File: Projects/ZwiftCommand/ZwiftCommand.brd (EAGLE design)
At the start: 47.4 x 21.2 mm, 17 parts, among them M1 DMP2165UW, U1 BAT-HLD-001-THM

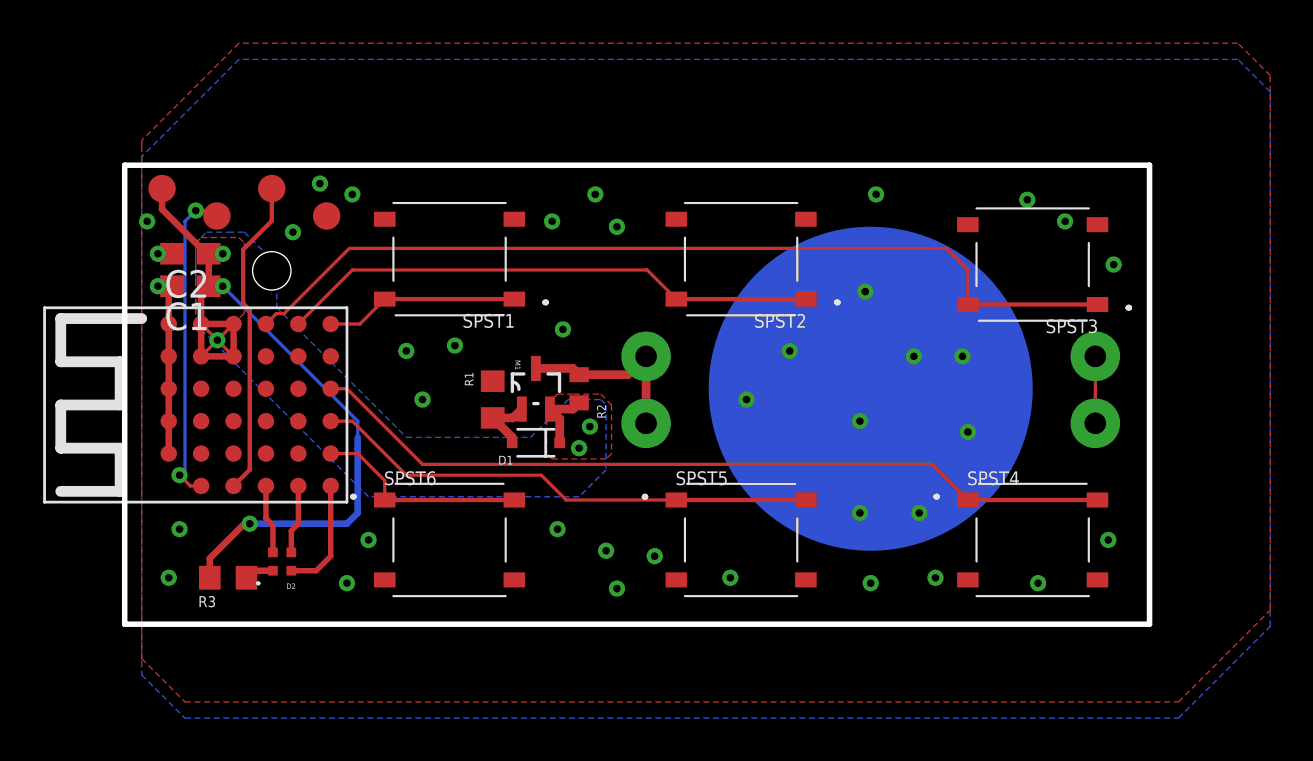
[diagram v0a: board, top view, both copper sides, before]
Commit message: ZwiftCommand with nRF52
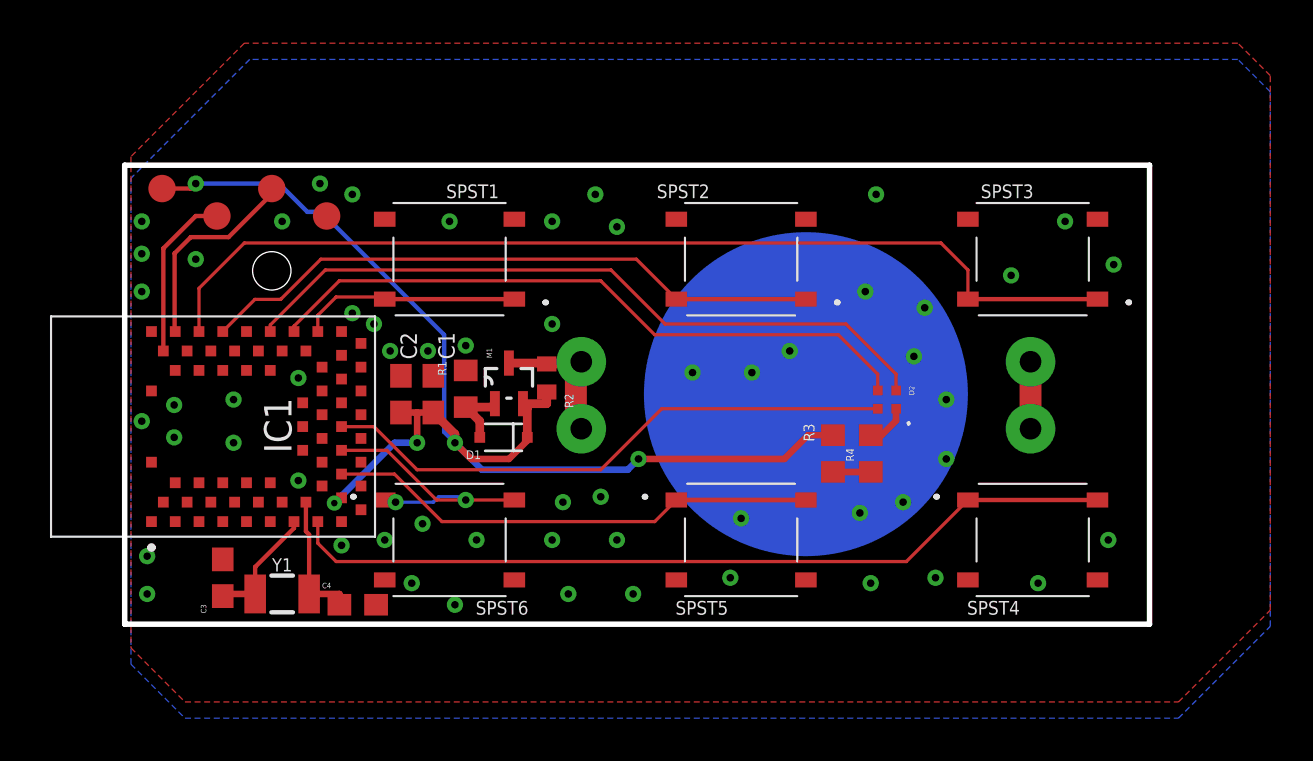
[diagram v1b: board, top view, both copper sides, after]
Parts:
- removed U$1: N5150, N5:N5150
- added C3, C4: (no value), resistor:C0603
- added IC1: BMD-340-A-R, Rigado:BMD340AR
- added R4: 300, resistor:R0603
- added Y1: 32.768kHz, SparkFun-Clocks:CRYSTAL-SMD-3.2X1.5MM
- moved D2 29.0 mm to (27.2, 12.5), turned to 270 degrees
- moved R3 28.6 mm to (24.8, 10.0), turned to 270 degrees
- moved C1 12.3 mm to (6.25, 12.8), turned to 90 degrees
- moved C2 11.7 mm to (4.75, 12.8), turned to 90 degrees
- moved U1 3.01 mm to (23.5, 12.8)
- moved R2 1.58 mm to (11.5, 13.5)
- moved D1 1.52 mm to (9.50, 10.8)
- moved R1 1.35 mm to (7.75, 13.0)
- moved M1 1.27 mm to (9.75, 13.2)
- moved SPST3 0.25 mm to (34.0, 19.0)
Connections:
- new net N$1: C3.1, IC1.13, Y1.P$1
- new net N$4: C4.1, IC1.14, Y1.P$2
- new net N$5: D2.1, R4.2
- net BTN1: now also IC1.31; no longer U$1.F6
- net BTN2: now also IC1.39; no longer U$1.E6
- net BTN3: now also IC1.41; no longer U$1.D6
- net BTN4: now also IC1.15; no longer U$1.F4
- net BTN5: now also IC1.19; no longer U$1.F3
- net BTN6: now also IC1.21; no longer U$1.F2
- net GND: now also C3.2, C4.2, IC1.1, IC1.16, IC1.18, IC1.2, IC1.29, IC1.3, IC1.30, IC1.4, IC1.45, IC1.46, IC1.47, IC1.5, IC1.55; no longer U$1.A2, U$1.A3, U$1.A4, U$1.A5, U$1.A6
- net LEDB: now also IC1.35; no longer U$1.F1
- net LEDG: now also IC1.33; no longer U$1.E1
- net LEDR: now also IC1.23; no longer U$1.D1
- net N$3: now also R4.1; no longer D2.1
- net SWDCLK: now also IC1.43; no longer U$1.C1
- net SWDIO: now also IC1.44; no longer U$1.B1
- net VDD: now also IC1.17; no longer U$1.B5, U$1.B6, U$1.C5, U$1.C6
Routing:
- net LEDB: track 5.35 -> 33.1 mm
- net LEDG: track 3.21 -> 30.7 mm
- net LEDR: track 3.21 -> 26.8 mm
- net VDD: track 43.0 -> 57.7 mm, vias 6 -> 5
- net GND: track 9.31 -> 0.00 mm, vias 39 -> 58
- net SWDIO: track 14.9 -> 8.43 mm, vias 2 -> 0
- net N$4: track 0.00 -> 6.21 mm
- net N$1: track 0.00 -> 5.64 mm
- net SWDCLK: track 14.8 -> 9.52 mm
- net BTN3: track 42.0 -> 46.3 mm
- net BTN2: track 25.1 -> 29.2 mm
- net BTN6: track 9.92 -> 13.3 mm, vias 0 -> 2
- net N$5: track 0.00 -> 2.00 mm
- net VBAT: track 11.8 -> 9.82 mm
- net BTN1: track 8.98 -> 10.2 mm
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- removed copper zone on layer 1, net VDD
- removed copper zone on layer 16, net VDD
